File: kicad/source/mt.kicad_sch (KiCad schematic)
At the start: 47 parts, among them IC1 MSPM0G3507SPMR, IC2 DAC082S085CIMMX_NOPB, IC3 IS62WV1288BLL-55QLI, IC4 MCP73831T-2ACI_OT, IC5 RT9167A-33GB, IC6 SN74HC148NSR, IC7 TLV9152IDR, IC8 TPS613222ADBVR, IC9 BQ29728DSER, J1 694106301002, J2 SJ1-3524N, J3 Conn_01x05_MountingPin, J4 Conn_01x09_MountingPin, Q1 CSD16406Q3, Q2 CSD16406Q3, U1 1043

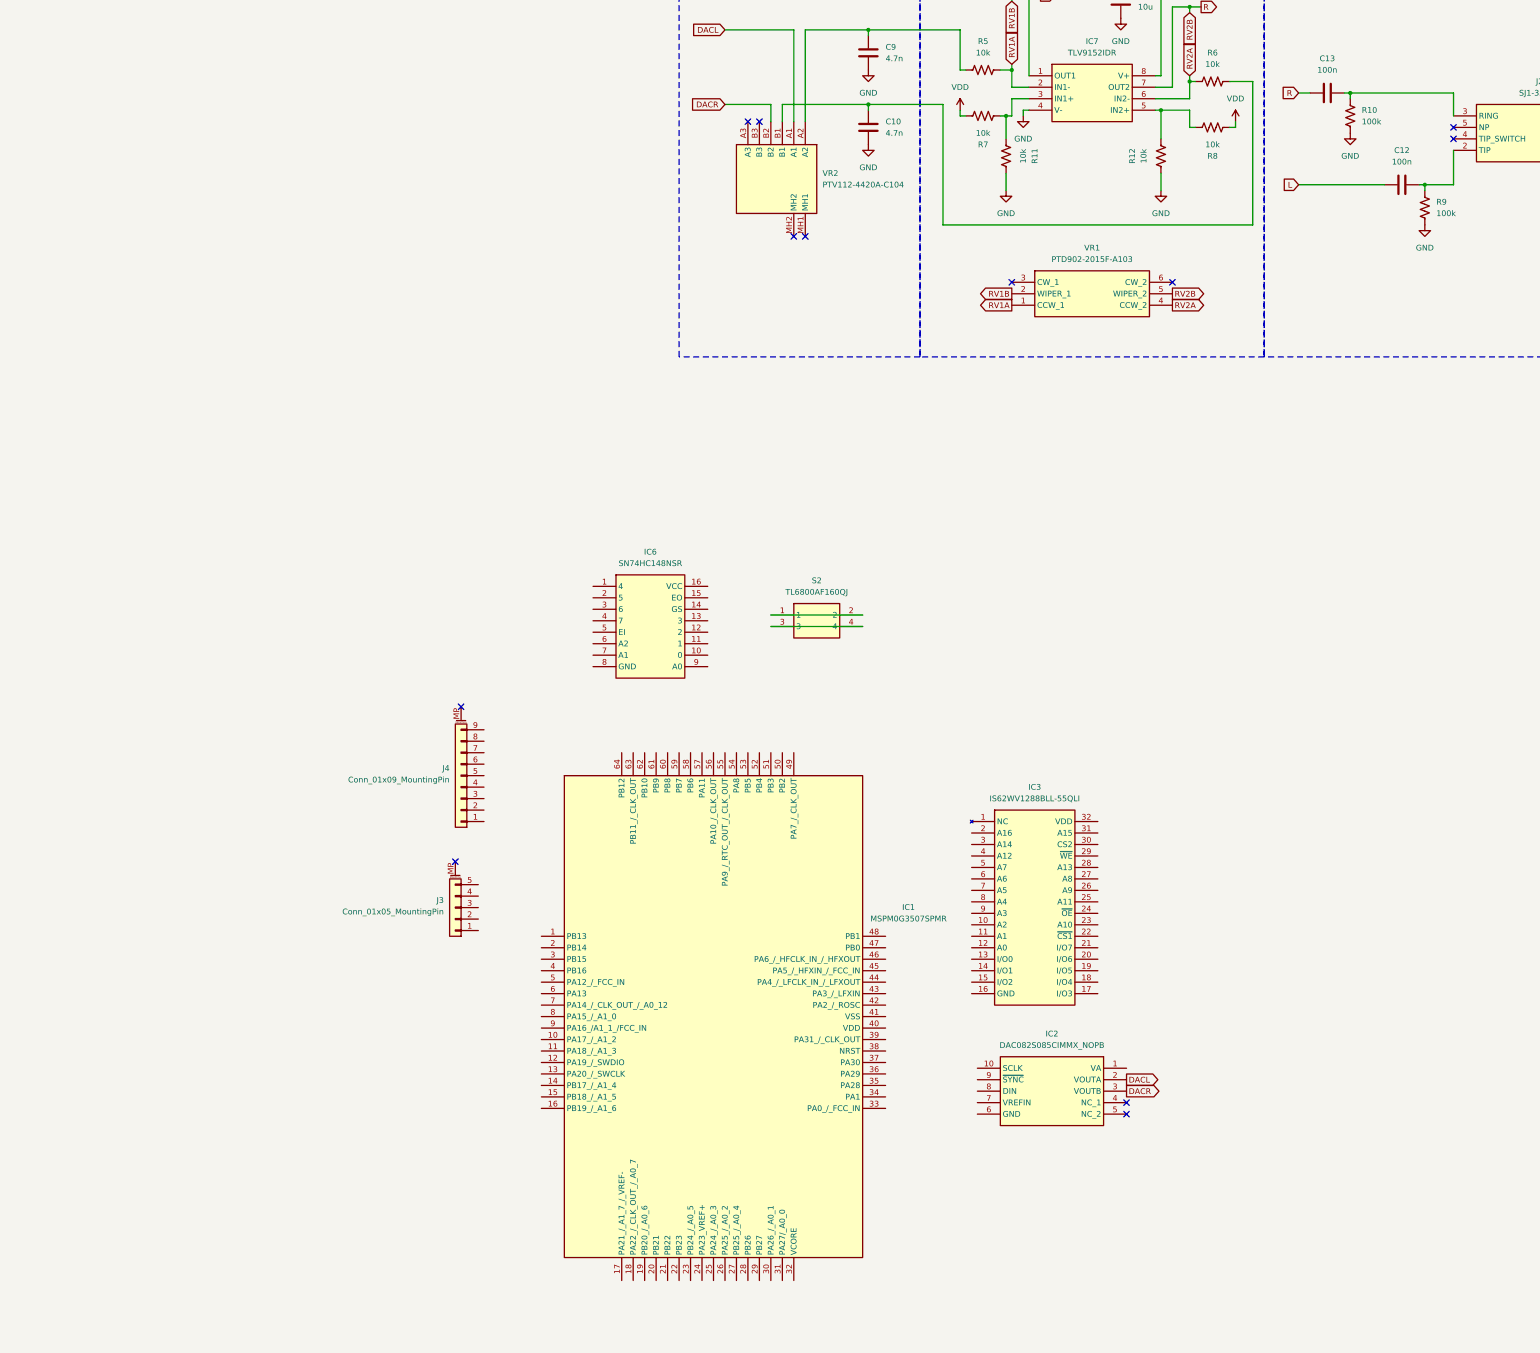
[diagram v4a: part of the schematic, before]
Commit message: revised some passives, started digital electronics schematic
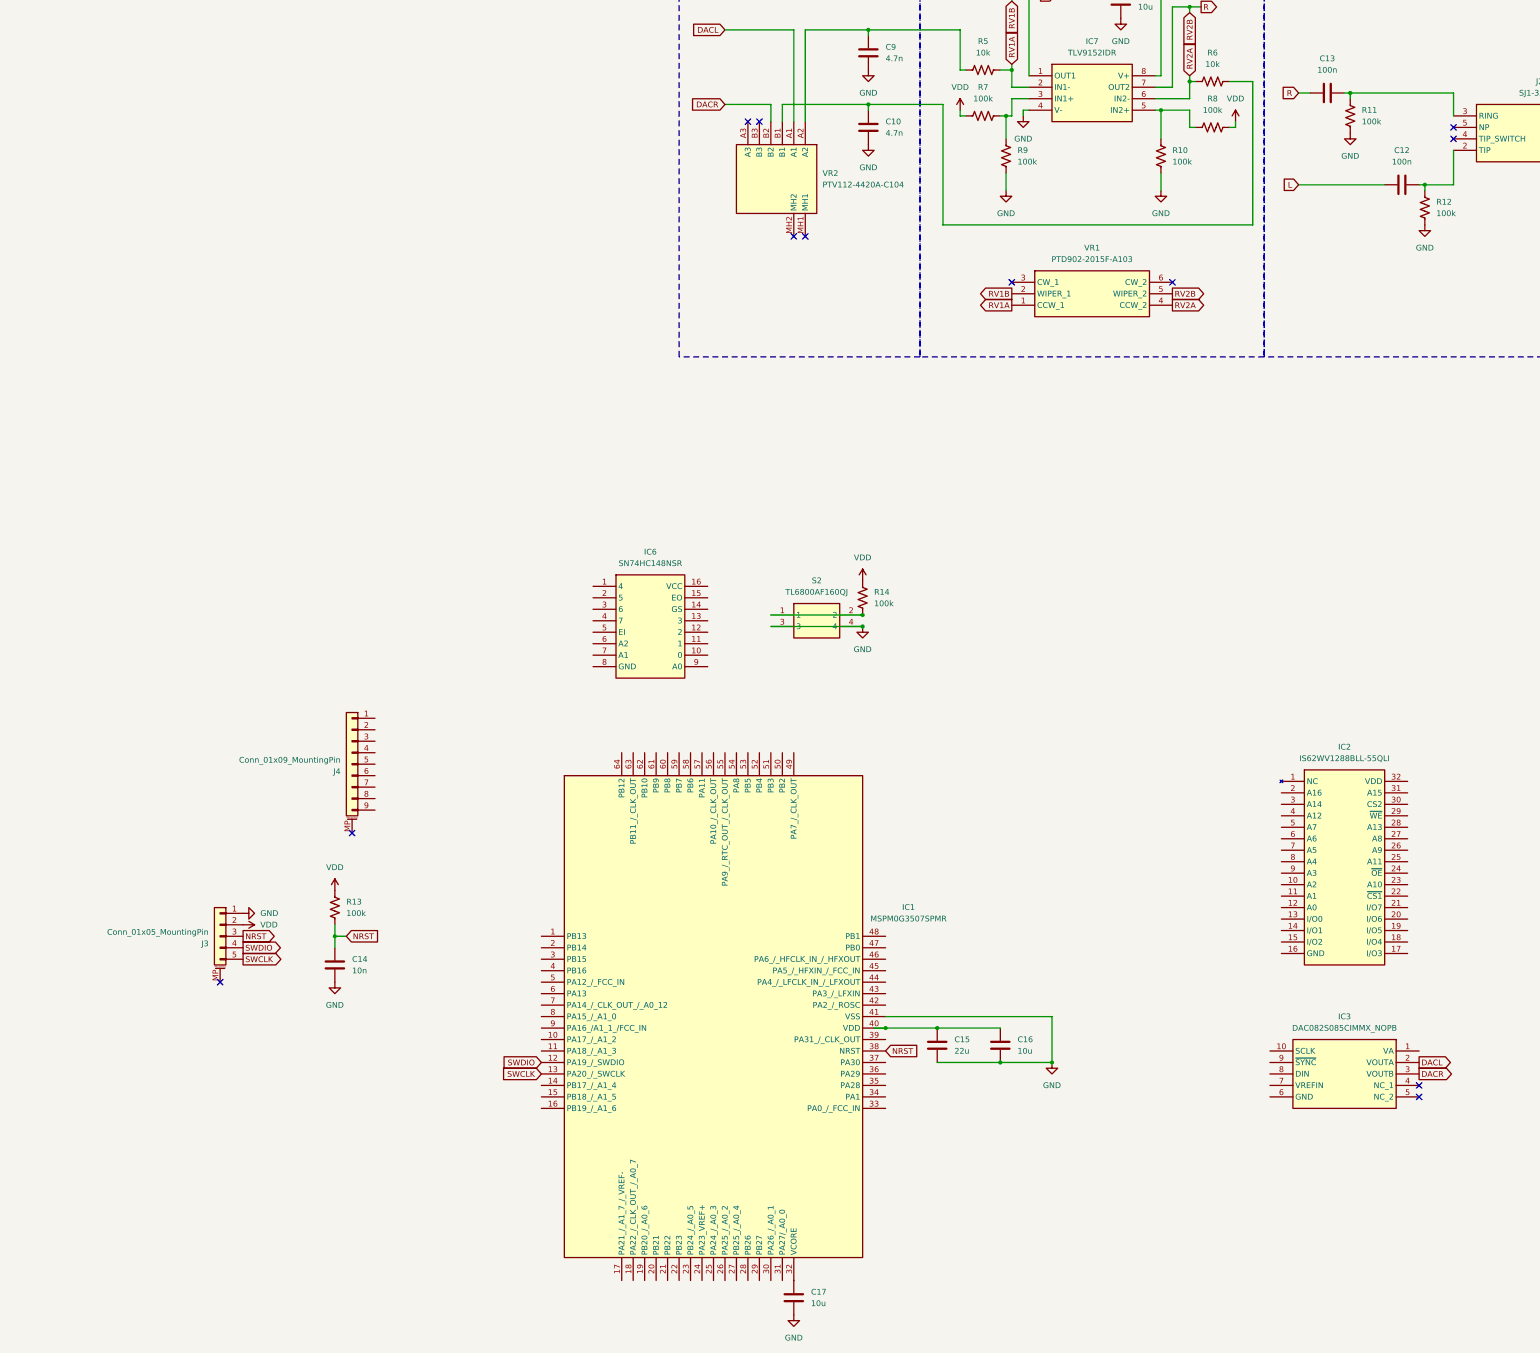
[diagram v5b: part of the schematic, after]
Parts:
- removed R11, R12: 10k, Resistor_SMD:R_0402_1005Metric, symbol Device:R_US
- added C14: 10n, Capacitor_SMD:C_0402_1005Metric, symbol Device:C
- added C15: 22u, Capacitor_SMD:C_0603_1608Metric, symbol Device:C
- added C16, C17: 10u, Capacitor_SMD:C_0402_1005Metric, symbol Device:C
- added R10, R13, R14, R9: 100k, Resistor_SMD:R_0402_1005Metric, symbol Device:R_US
- C1, C11, C2, C4, C8: footprint Capacitor_SMD:C_0603_1608Metric -> Capacitor_SMD:C_0402_1005Metric; JLCPCB C19702 -> C15525
- IC1: JLCPCB (none) -> C22389960
- IC2: renamed from IC3; JLCPCB (none) -> C1351025
- IC3: renamed from IC2; JLCPCB (none) -> C2860238
- IC6: JLCPCB (none) -> C2653280
- R7, R8: value 10k -> 100k; JLCPCB C25744 -> C25741
- VR1: footprint PTD9022015FA103 -> PTD902-2015F-A103:PTD9022015FA103
- VR2: footprint PTV1124420AC104 -> PTV112-4420A-C104:PTV1124420AC104
- renumbered R10 to R11, R9 to R12
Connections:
- net GND: now also IC1.41 (VSS), J3.1 (Pin_1), S2.3, S2.4, C14.2, C15.2, C16.2, C17.2, R10.2, R9.2
- net VDD: now also J3.2 (Pin_2), R13.1, R14.1
- net at IC7.3 (IN1+), R7.2: now also R9.1
- net at IC7.5 (IN2+), R8.1: now also R10.1
- net NRST: now reaches J3.3 (Pin_3)
- net NRST: now also IC1.38 (NRST), C14.1, R13.2
- net SWDIO: now reaches J3.4 (Pin_4)
- net SWDIO: now also IC1.12 (PA19_/_SWDIO)
- net SWCLK: now reaches J3.5 (Pin_5)
- net SWCLK: now also IC1.13 (PA20_/_SWCLK)
- net at IC1.32 (VCORE): now also C17.1
- net at IC1.40 (VDD): now also C15.1, C16.1
- net at S2.1, S2.2: now also R14.2
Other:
- moved on the sheet: IC2, IC3, J3, J4

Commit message: started sram schematic
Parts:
- added C18: 22u, Capacitor_SMD:C_0603_1608Metric, symbol Device:C
- added C19: 10u, Capacitor_SMD:C_0402_1005Metric, symbol Device:C
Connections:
- net GND: now also IC2.16 (GND), C18.2, C19.2
- net A13: now reaches IC1.1 (PB13)
- net A13: now also IC2.28 (A13)
- net A14: now reaches IC1.2 (PB14)
- net A14: now also IC2.3 (A14)
- net A15: now reaches IC1.3 (PB15)
- net A15: now also IC2.31 (A15)
- net A16: now reaches IC1.4 (PB16)
- net A16: now also IC2.2 (A16)
- net A0: now reaches IC1.47 (PB0)
- net A0: now also IC2.12 (A0)
- net A1: now reaches IC1.48 (PB1)
- net A1: now also IC2.11 (A1)
- net A2: now reaches IC1.50 (PB2)
- net A2: now also IC2.10 (A2)
- net A3: now reaches IC1.51 (PB3)
- net A3: now also IC2.9 (A3)
- net A4: now reaches IC1.52 (PB4)
- net A4: now also IC2.8 (A4)
- net A5: now reaches IC1.53 (PB5)
- net A5: now also IC2.7 (A5)
- net A6: now reaches IC1.58 (PB6)
- net A6: now also IC2.6 (A6)
- net A7: now reaches IC1.59 (PB7)
- net A7: now also IC2.5 (A7)
- net A8: now reaches IC1.60 (PB8)
- net A8: now also IC2.27 (A8)
- net A9: now reaches IC1.61 (PB9)
- net A9: now also IC2.26 (A9)
- net A10: now reaches IC1.62 (PB10)
- net A10: now also IC2.23 (A10)
- net A11: now reaches IC1.63 (PB11_/_CLK_OUT)
- net A11: now also IC2.25 (A11)
- net A12: now reaches IC1.64 (PB12)
- net A12: now also IC2.4 (A12)
- net at IC2.32 (VDD): now also C18.1, C19.1
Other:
- moved on the sheet: IC2, IC6, J4, R14, S2

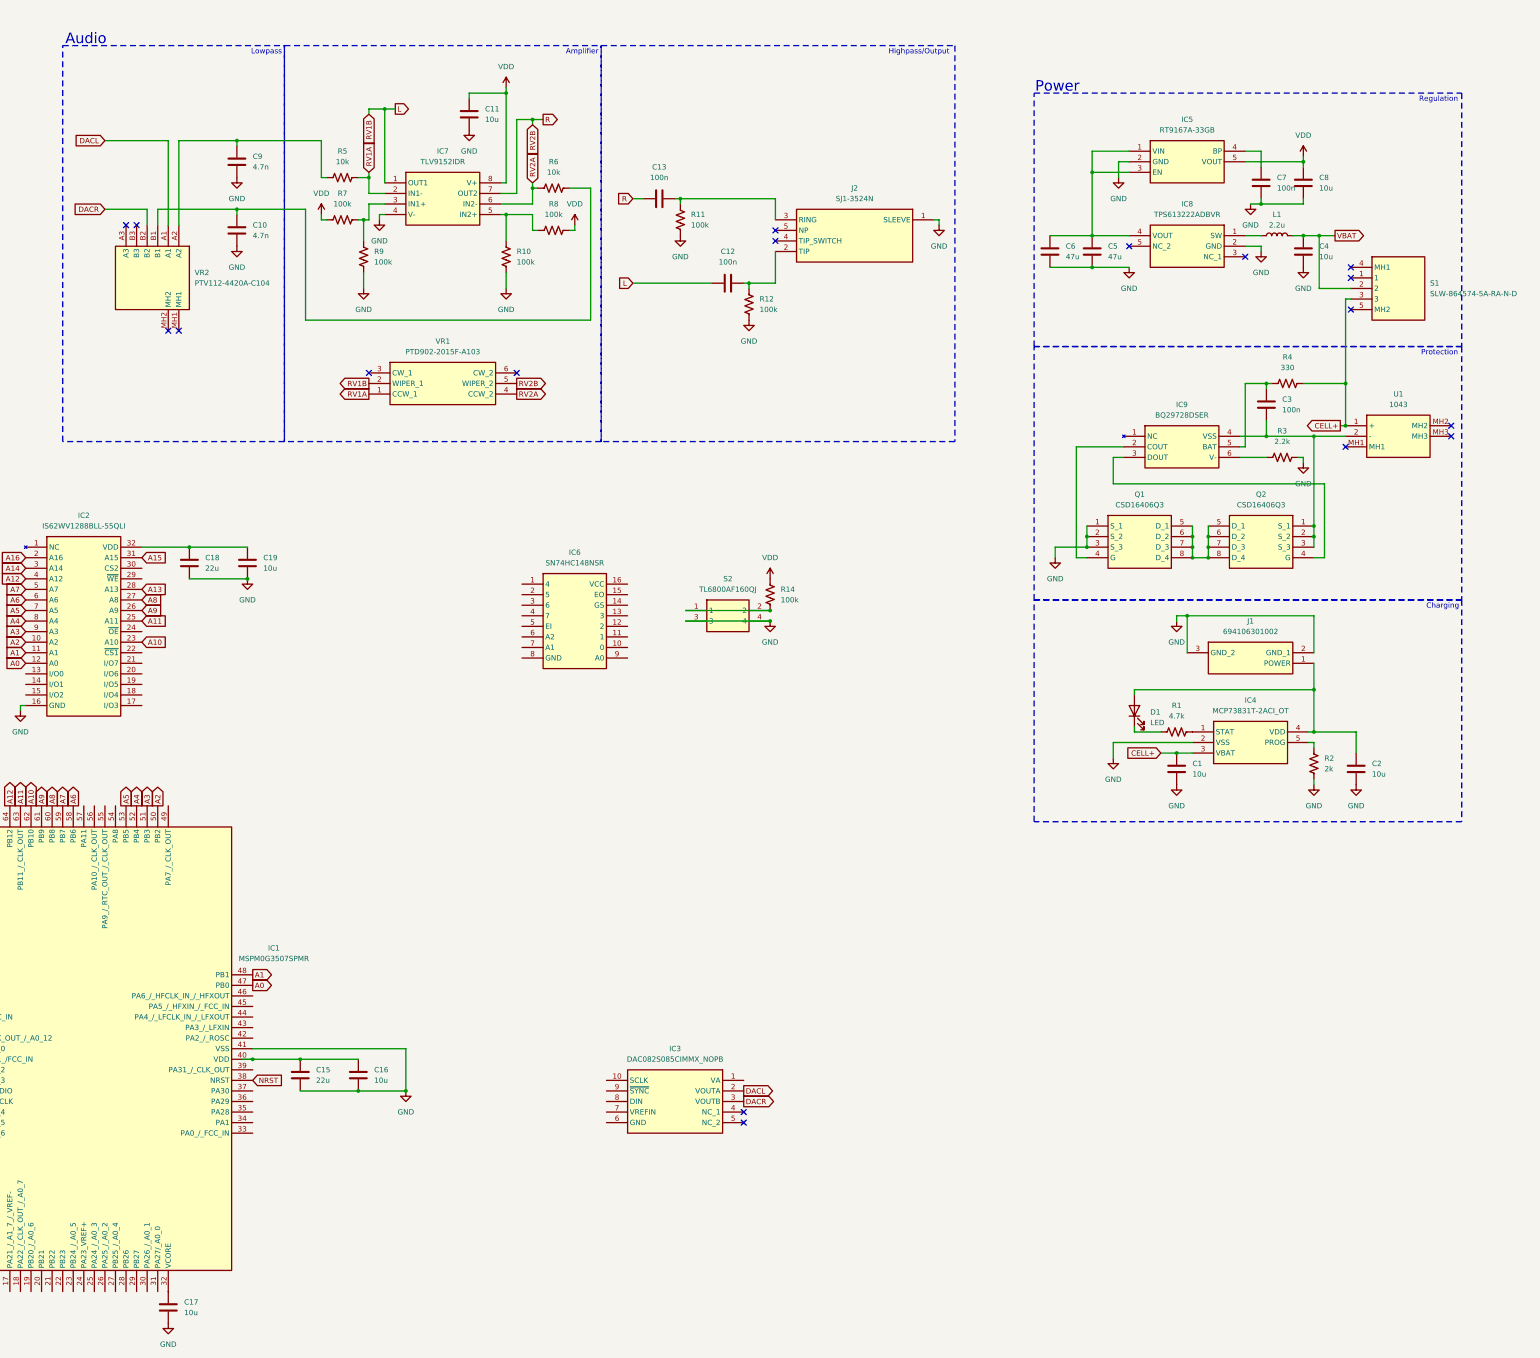
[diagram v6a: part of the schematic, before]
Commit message: simplified power electronics
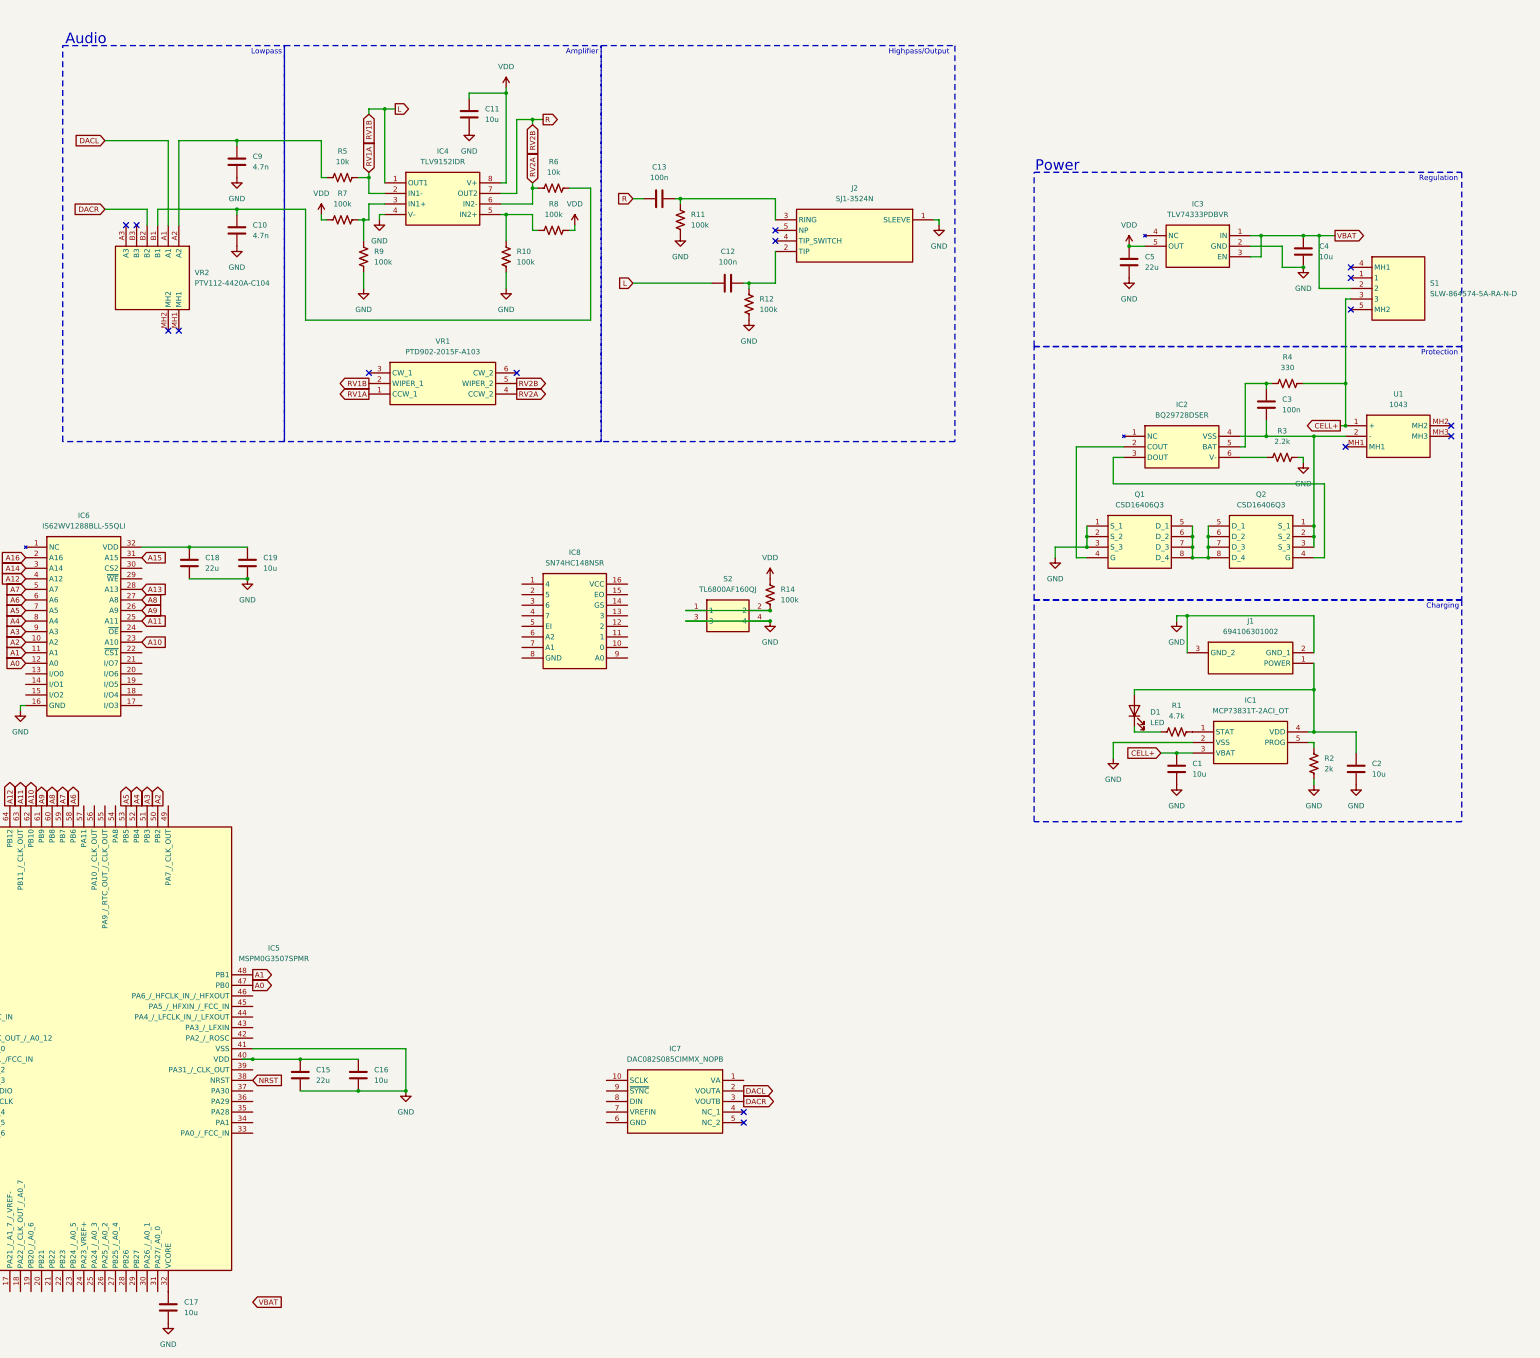
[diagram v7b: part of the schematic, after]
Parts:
- removed C6: 47u, Capacitor_SMD:C_0805_2012Metric, symbol Device:C
- removed C7: 100n, Capacitor_SMD:C_1206_3216Metric, symbol Device:C
- removed C8: 10u, Capacitor_SMD:C_0402_1005Metric, symbol Device:C
- removed IC5: RT9167A-33GB, RT9167A-33GB:SOT94P279X130-5N, symbol RT9167A-33GB:RT9167A-33GB
- removed IC8: TPS613222ADBVR, TPS613222ADBVR:SOT95P280X145-5N, symbol TPS613222ADBVR:TPS613222ADBVR
- removed L1: 2.2u, Inductor_SMD:L_1008_2520Metric, symbol Device:L
- added IC3: TLV74333PDBVR, TLV74333PDBVR:SOT95P280X145-5N, symbol TLV74333PDBVR:TLV74333PDBVR
- C5: value 47u -> 22u; footprint Capacitor_SMD:C_0805_2012Metric -> Capacitor_SMD:C_0603_1608Metric; JLCPCB C16780 -> C59461
- renumbered IC4 to IC1, IC9 to IC2, IC7 to IC4, IC1 to IC5, IC2 to IC6, IC3 to IC7, IC6 to IC8
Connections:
- net GND: now also IC3.2 (GND)
- net VBAT: now also IC3.1 (IN), IC3.3 (EN)
- net VDD: now also C5.1, IC3.5 (OUT)
- no-connect marks 20 -> 18
